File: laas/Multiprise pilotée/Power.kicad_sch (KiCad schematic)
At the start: 16 parts, among them J1 Conn_01x03, J2 Conn_01x02, J3 Conn_01x02, J4 Conn_01x02, J5 Conn_01x02, J6 Conn_01x03, K1 Omron Relay, K2 Omron Relay, K3 Omron Relay, K4 Omron Relay, U1 MAX4820xUP, U3 TPS75933KC

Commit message: Sauvegarde du travail en cours
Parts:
- J2: footprint Connector_Wago:Wago_734-132_1x02_P3.50mm_Vertical -> Connector_Wuerth:Wuerth_WR-WTB_64800211622_1x02_P1.50mm_Vertical
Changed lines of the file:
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@@
       (effects (font (size 1.27 1.27)) hide)
     )
-    (property "Footprint" "Connector_Wago:Wago_734-132_1x02_P3.50mm_Vertical" (at 170.18 139.7 0)
+    (property "Footprint" "Connector_Wuerth:Wuerth_WR-WTB_64800211622_1x02_P1.50mm_Vertical" (at 170.18 139.7 0)
       (effects (font (size 1.27 1.27)) hide)
     )

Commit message: Commit de propreté
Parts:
- C1: footprint Capacitor_THT:CP_Radial_D6.3mm_P2.50mm -> Capacitor_THT:CP_Radial_D5.0mm_P2.00mm
- J1, J6: footprint Connector_Wago:Wago_734-133_1x03_P3.50mm_Vertical -> Borniers:5442183
- J2: footprint Connector_Wuerth:Wuerth_WR-WTB_64800211622_1x02_P1.50mm_Vertical -> Borniers:5442170
- J3, J4, J5: footprint Connector_Wago:Wago_734-132_1x02_P3.50mm_Vertical -> Borniers:5442170
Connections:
- net Relay_1: now also U1.19 (OUT2); no longer U1.20 (OUT1)
- net Relay_2: now also U1.16 (OUT4); no longer U1.19 (OUT2)
- net Relay_4: now also U1.20 (OUT1); no longer U1.16 (OUT4)
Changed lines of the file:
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@@
     (stroke (width 0) (type default))
-  )
-  (label "Relay_1" (at 99.06 101.6 180) (fields_autoplaced)
-    (effects (font (size 1.27 1.27)) (justify right bottom))
-  )
-  (label "Relay_2" (at 99.06 104.14 180) (fields_autoplaced)
-    (effects (font (size 1.27 1.27)) (justify right bottom))
   )
   (label "Relay_4" (at 242.57 109.22 90) (fields_autoplaced)
@@
     (effects (font (size 1.27 1.27)) (justify left bottom))
   )
+  (label "Relay_1" (at 99.06 104.14 180) (fields_autoplaced)
+    (effects (font (size 1.27 1.27)) (justify right bottom))
+  )
+  (label "Relay_2" (at 99.06 109.22 180) (fields_autoplaced)
+    (effects (font (size 1.27 1.27)) (justify right bottom))
+  )
   (label "Relay_3" (at 213.36 109.22 90) (fields_autoplaced)
     (effects (font (size 1.27 1.27)) (justify left bottom))
   )
-  (label "Relay_4" (at 99.06 109.22 180) (fields_autoplaced)
+  (label "Relay_4" (at 99.06 101.6 180) (fields_autoplaced)
     (effects (font (size 1.27 1.27)) (justify right bottom))
   )
@@
       (effects (font (size 1.27 1.27)) hide)
     )
-    (property "Footprint" "Connector_Wago:Wago_734-132_1x02_P3.50mm_Vertical" (at 261.62 139.7 0)
+    (property "Footprint" "Borniers:5442170" (at 261.62 139.7 0)
       (effects (font (size 1.27 1.27)) hide)
     )
@@
       (effects (font (size 1.27 1.27)) (justify left))
     )
-    (property "Footprint" "Capacitor_THT:CP_Radial_D6.3mm_P2.50mm" (at 157.1752 45.72 0)
+    (property "Footprint" "Capacitor_THT:CP_Radial_D5.0mm_P2.00mm" (at 157.1752 45.72 0)
       (effects (font (size 1.27 1.27)) hide)
     )
@@
       (effects (font (size 1.27 1.27)) hide)
     )
-    (property "Footprint" "Connector_Wago:Wago_734-133_1x03_P3.50mm_Vertical" (at 30.48 40.64 0)
+    (property "Footprint" "Borniers:5442183" (at 30.48 40.64 0)
       (effects (font (size 1.27 1.27)) hide)
     )
@@
       (effects (font (size 1.27 1.27)) hide)
     )
-    (property "Footprint" "Connector_Wago:Wago_734-132_1x02_P3.50mm_Vertical" (at 231.14 139.7 0)
+    (property "Footprint" "Borniers:5442170" (at 231.14 139.7 0)
       (effects (font (size 1.27 1.27)) hide)
     )
@@
       (effects (font (size 1.27 1.27)) hide)
     )
-    (property "Footprint" "Connector_Wago:Wago_734-132_1x02_P3.50mm_Vertical" (at 201.93 139.7 0)
+    (property "Footprint" "Borniers:5442170" (at 201.93 139.7 0)
       (effects (font (size 1.27 1.27)) hide)
     )
@@
       (effects (font (size 1.27 1.27)) hide)
     )
-    (property "Footprint" "Connector_Wago:Wago_734-133_1x03_P3.50mm_Vertical" (at 30.48 54.61 0)
+    (property "Footprint" "Borniers:5442183" (at 30.48 54.61 0)
       (effects (font (size 1.27 1.27)) hide)
     )
@@
       (effects (font (size 1.27 1.27)) hide)
     )
-    (property "Footprint" "Connector_Wuerth:Wuerth_WR-WTB_64800211622_1x02_P1.50mm_Vertical" (at 170.18 139.7 0)
-      (effects (font (size 1.27 1.27)) hide)
-    )
+    (property "Footprint" "Borniers:5442170" (at 170.18 139.7 0)
+      (effects (font (size 1.27 1.27)) hide)
+    )

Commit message: Doc api
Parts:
- added H1, H2, H3, H4: MountingHole, MountingHole:MountingHole_4.3mm_M4, symbol Mechanical:MountingHole
- PS2: value MPM-45 -> MPM-30-5; footprint Multiprise pilotée:Converter_ACDC_MeanWell_MPM-45-xx_THT -> Multiprise pilotée:Converter_ACDC_MeanWell_MPM-30-xx_THT
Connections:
- net +5V: now also U1.2 (~{SET})
- net R3_L: now reaches J4.1 (Pin_1), K3.14
- net R3_N: now reaches J4.2 (Pin_2), K3.24
- net R1_L: now reaches J2.1 (Pin_1), K1.14
- net R1_N: now reaches J2.2 (Pin_2), K1.24
- net R4_L: now reaches J5.1 (Pin_1), K4.14
- net R4_N: now reaches J5.2 (Pin_2), K4.24
- net R2_L: now reaches J3.1 (Pin_1), K2.14
- net R2_N: now reaches J3.2 (Pin_2), K2.24
- no-connect marks 14 -> 13
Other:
- title: (none) -> AC & Relay
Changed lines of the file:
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@@
 (kicad_sch (version 20230121) (generator eeschema)
   (paper "A4")
+  (title_block
+    (title "AC & Relay")
+    (date "2024-04-26")
+    (rev "1.2")
+  )
   (junction (at 39.37 52.07) (diameter 0) (color 0 0 0 0)
   )
@@
   (no_connect (at 81.28 111.76))
   (no_connect (at 176.53 106.68))
-  (no_connect (at 55.88 104.14))
   (no_connect (at 266.7 116.84))
   (no_connect (at 207.01 116.84))
@@
     (stroke (width 0) (type default))
   )
+  (wire (pts (xy 49.53 104.14) (xy 49.53 87.63))
+    (stroke (width 0) (type default))
+  )
   (wire (pts (xy 81.28 109.22) (xy 99.06 109.22))
     (stroke (width 0) (type default))
@@
     (stroke (width 0) (type default))
   )
+  (wire (pts (xy 49.53 87.63) (xy 68.58 87.63))
+    (stroke (width 0) (type default))
+  )
   (wire (pts (xy 152.4 99.06) (xy 152.4 109.22))
     (stroke (width 0) (type default))
@@
     (stroke (width 0) (type default))
   )
+  (wire (pts (xy 55.88 104.14) (xy 49.53 104.14))
+    (stroke (width 0) (type default))
+  )
   (wire (pts (xy 245.11 91.44) (xy 245.11 119.38))
     (stroke (width 0) (type default))
@@
   (wire (pts (xy 161.29 99.06) (xy 152.4 99.06))
     (stroke (width 0) (type default))
+  )
+  (label "R3_N" (at 228.6 134.62 90) (fields_autoplaced)
+    (effects (font (size 1.27 1.27)) (justify left bottom))
   )
   (label "Relay_4" (at 242.57 109.22 90) (fields_autoplaced)
     (effects (font (size 1.27 1.27)) (justify left bottom))
   )
+  (label "R4_N" (at 259.08 134.62 90) (fields_autoplaced)
+    (effects (font (size 1.27 1.27)) (justify left bottom))
+  )
+  (label "R1_N" (at 167.64 134.62 90) (fields_autoplaced)
+    (effects (font (size 1.27 1.27)) (justify left bottom))
+  )
+  (label "R4_L" (at 269.24 132.08 0) (fields_autoplaced)
+    (effects (font (size 1.27 1.27)) (justify left bottom))
+  )
   (label "Relay_1" (at 152.4 109.22 90) (fields_autoplaced)
     (effects (font (size 1.27 1.27)) (justify left bottom))
   )
+  (label "R1_L" (at 179.07 132.08 0) (fields_autoplaced)
+    (effects (font (size 1.27 1.27)) (justify left bottom))
+  )
   (label "Relay_3" (at 99.06 106.68 180) (fields_autoplaced)
     (effects (font (size 1.27 1.27)) (justify right bottom))
@@
     (effects (font (size 1.27 1.27)) (justify left bottom))
   )
+  (label "R2_L" (at 210.82 132.08 0) (fields_autoplaced)
+    (effects (font (size 1.27 1.27)) (justify left bottom))
+  )
   (label "Relay_1" (at 99.06 104.14 180) (fields_autoplaced)
     (effects (font (size 1.27 1.27)) (justify right bottom))
@@
     (effects (font (size 1.27 1.27)) (justify right bottom))
   )
+  (label "R3_L" (at 238.76 132.08 0) (fields_autoplaced)
+    (effects (font (size 1.27 1.27)) (justify left bottom))
+  )
+  (label "R2_N" (at 199.39 134.62 90) (fields_autoplaced)
+    (effects (font (size 1.27 1.27)) (justify left bottom))
+  )
   (hierarchical_label "~{CS_Relay}" (shape input) (at 43.18 114.3 180) (fields_autoplaced)
     (effects (font (size 1.27 1.27)) (justify right))
@@
         (path "/ad17dd83-c10a-426e-803d-3b2dda0cc379/ff439e0e-b879-40be-a702-6e5da693c895"
           (reference "#PWR04") (unit 1)
+        )
+      )
+    )
+  )
+  (symbol (lib_id "Mechanical:MountingHole") (at 36.83 194.31 0) (unit 1)
+    (in_bom yes) (on_board yes) (dnp no) (fields_autoplaced)
+    (property "Reference" "H4" (at 39.37 193.04 0)
+      (effects (font (size 1.27 1.27)) (justify left))
+    )
+    (property "Value" "MountingHole" (at 39.37 195.58 0)
+      (effects (font (size 1.27 1.27)) (justify left) hide)
+    )
+    (property "Footprint" "MountingHole:MountingHole_4.3mm_M4" (at 36.83 194.31 0)
+      (effects (font (size 1.27 1.27)) hide)
+    )
+    (property "Datasheet" "~" (at 36.83 194.31 0)
+      (effects (font (size 1.27 1.27)) hide)
+    )
+    (instances
+      (project "Multiprise pilotée"
+        (path "/ad17dd83-c10a-426e-803d-3b2dda0cc379/ff439e0e-b879-40be-a702-6e5da693c895"
+          (reference "H4") (unit 1)
         )
       )
@@
     )
   )
+  (symbol (lib_id "Mechanical:MountingHole") (at 36.83 184.15 0) (unit 1)
+    (in_bom yes) (on_board yes) (dnp no) (fields_autoplaced)
+    (property "Reference" "H2" (at 39.37 182.88 0)
+      (effects (font (size 1.27 1.27)) (justify left))
+    )
+    (property "Value" "MountingHole" (at 39.37 185.42 0)
+      (effects (font (size 1.27 1.27)) (justify left) hide)
+    )
+    (property "Footprint" "MountingHole:MountingHole_4.3mm_M4" (at 36.83 184.15 0)
+      (effects (font (size 1.27 1.27)) hide)
+    )
+    (property "Datasheet" "~" (at 36.83 184.15 0)
+      (effects (font (size 1.27 1.27)) hide)
+    )
+    (instances
+      (project "Multiprise pilotée"
+        (path "/ad17dd83-c10a-426e-803d-3b2dda0cc379/ff439e0e-b879-40be-a702-6e5da693c895"
+          (reference "H2") (unit 1)
+        )
+      )
+    )
+  )
   (symbol (lib_id "Connector_Generic:Conn_01x02") (at 261.62 139.7 270) (unit 1)
     (in_bom yes) (on_board yes) (dnp no) (fields_autoplaced)
@@
       (effects (font (size 1.27 1.27)))
     )
-    (property "Value" "MPM-45" (at 58.42 34.29 0)
-      (effects (font (size 1.27 1.27)))
-    )
-    (property "Footprint" "Multiprise pilotée:Converter_ACDC_MeanWell_MPM-45-xx_THT" (at 58.42 48.26 0)
+    (property "Value" "MPM-30-5" (at 58.42 34.29 0)
+      (effects (font (size 1.27 1.27)))
+    )
+    (property "Footprint" "Multiprise pilotée:Converter_ACDC_MeanWell_MPM-30-xx_THT" (at 58.42 48.26 0)
       (effects (font (size 1.27 1.27)) hide)
     )
@@
     )
   )
+  (symbol (lib_id "Mechanical:MountingHole") (at 36.83 189.23 0) (unit 1)
+    (in_bom yes) (on_board yes) (dnp no) (fields_autoplaced)
+    (property "Reference" "H3" (at 39.37 187.96 0)
+      (effects (font (size 1.27 1.27)) (justify left))
+    )
+    (property "Value" "MountingHole" (at 39.37 190.5 0)
+      (effects (font (size 1.27 1.27)) (justify left) hide)
+    )
+    (property "Footprint" "MountingHole:MountingHole_4.3mm_M4" (at 36.83 189.23 0)
+      (effects (font (size 1.27 1.27)) hide)
+    )
+    (property "Datasheet" "~" (at 36.83 189.23 0)
+      (effects (font (size 1.27 1.27)) hide)
+    )
+    (instances
+      (project "Multiprise pilotée"
+        (path "/ad17dd83-c10a-426e-803d-3b2dda0cc379/ff439e0e-b879-40be-a702-6e5da693c895"
+          (reference "H3") (unit 1)
+        )
+      )
+    )
+  )
   (symbol (lib_id "Multiprise pilotée:TPS75933KC") (at 124.46 40.64 0) (unit 1)
     (in_bom yes) (on_board yes) (dnp no) (fields_autoplaced)
@@
         )
       )
+    )
+  )
+  (symbol (lib_id "Mechanical:MountingHole") (at 36.83 179.07 0) (unit 1)
+    (in_bom yes) (on_board yes) (dnp no) (fields_autoplaced)
+    (property "Reference" "H1" (at 39.37 177.8 0)
+      (effects (font (size 1.27 1.27)) (justify left))
+    )
+    (property "Value" "MountingHole" (at 39.37 180.34 0)
+      (effects (font (size 1.27 1.27)) (justify left) hide)
+    )
+    (property "Footprint" "MountingHole:MountingHole_4.3mm_M4" (at 36.83 179.07 0)
+      (effects (font (size 1.27 1.27)) hide)
+    )
+    (property "Datasheet" "~" (at 36.83 179.07 0)
+      (effects (font (size 1.27 1.27)) hide)
+    )
+    (instances
+      (project "Multiprise pilotée"
+        (path "/ad17dd83-c10a-426e-803d-3b2dda0cc379/ff439e0e-b879-40be-a702-6e5da693c895"
+          (reference "H1") (unit 1)
+        )
+      )

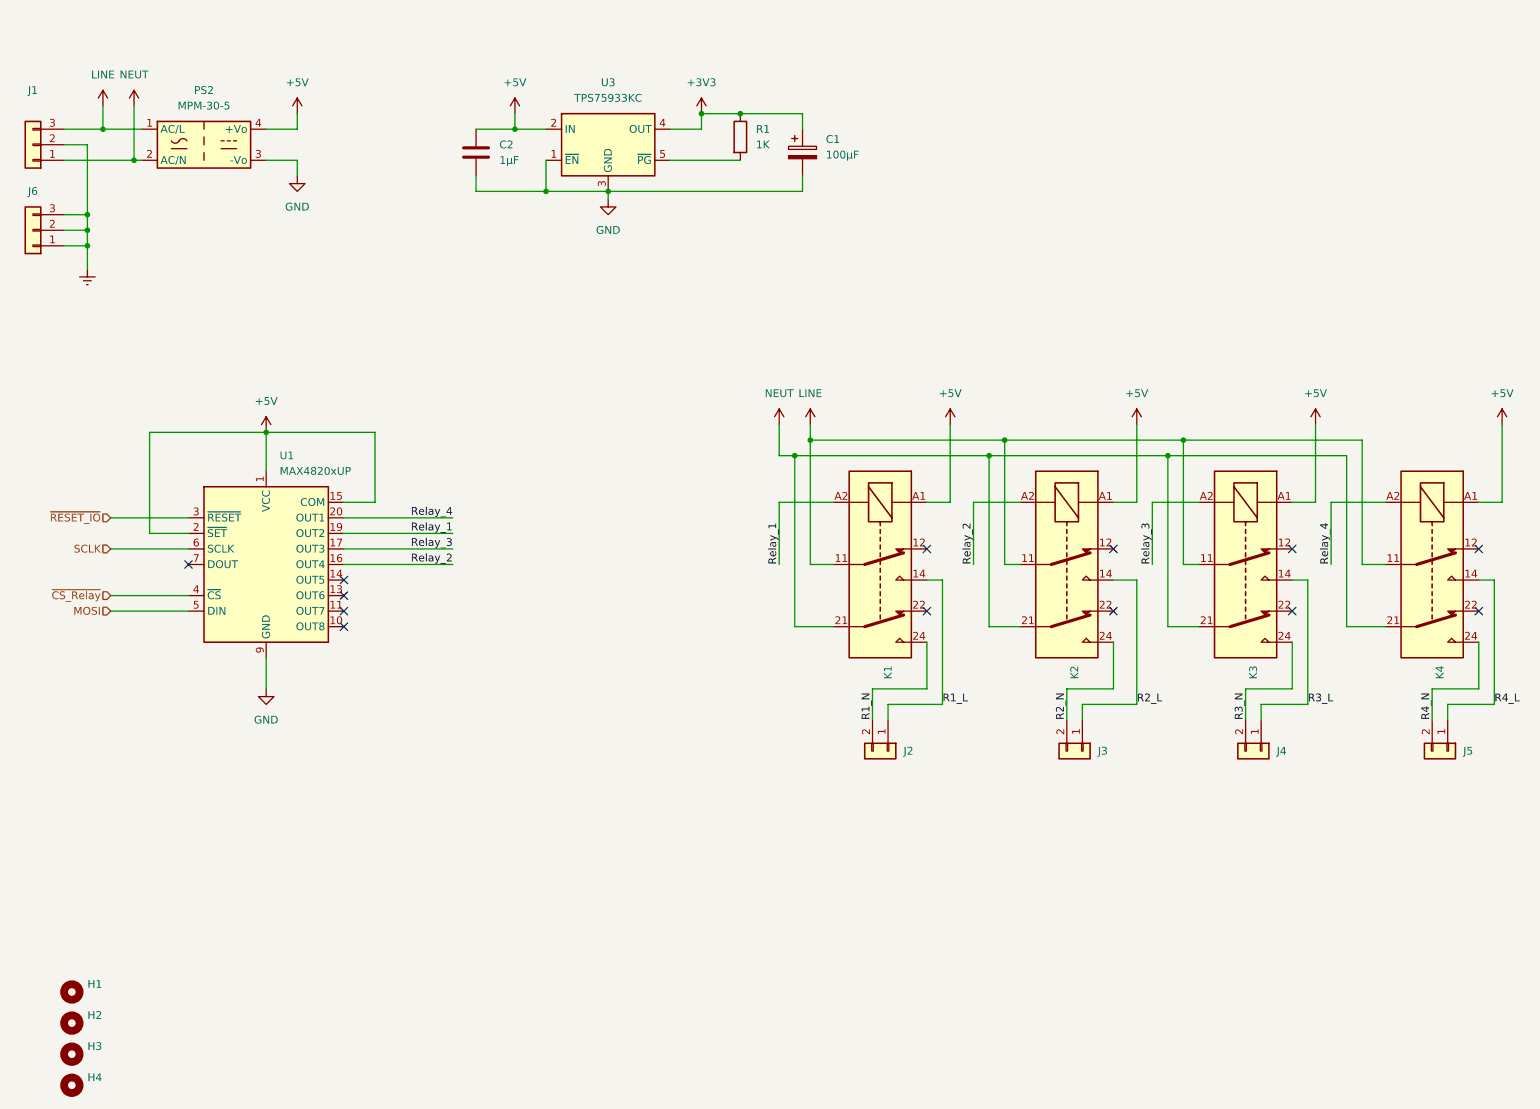
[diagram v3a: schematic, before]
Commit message: Nouvelle version PCB multiprise 1.3 avec suppresion des alim vpol et var
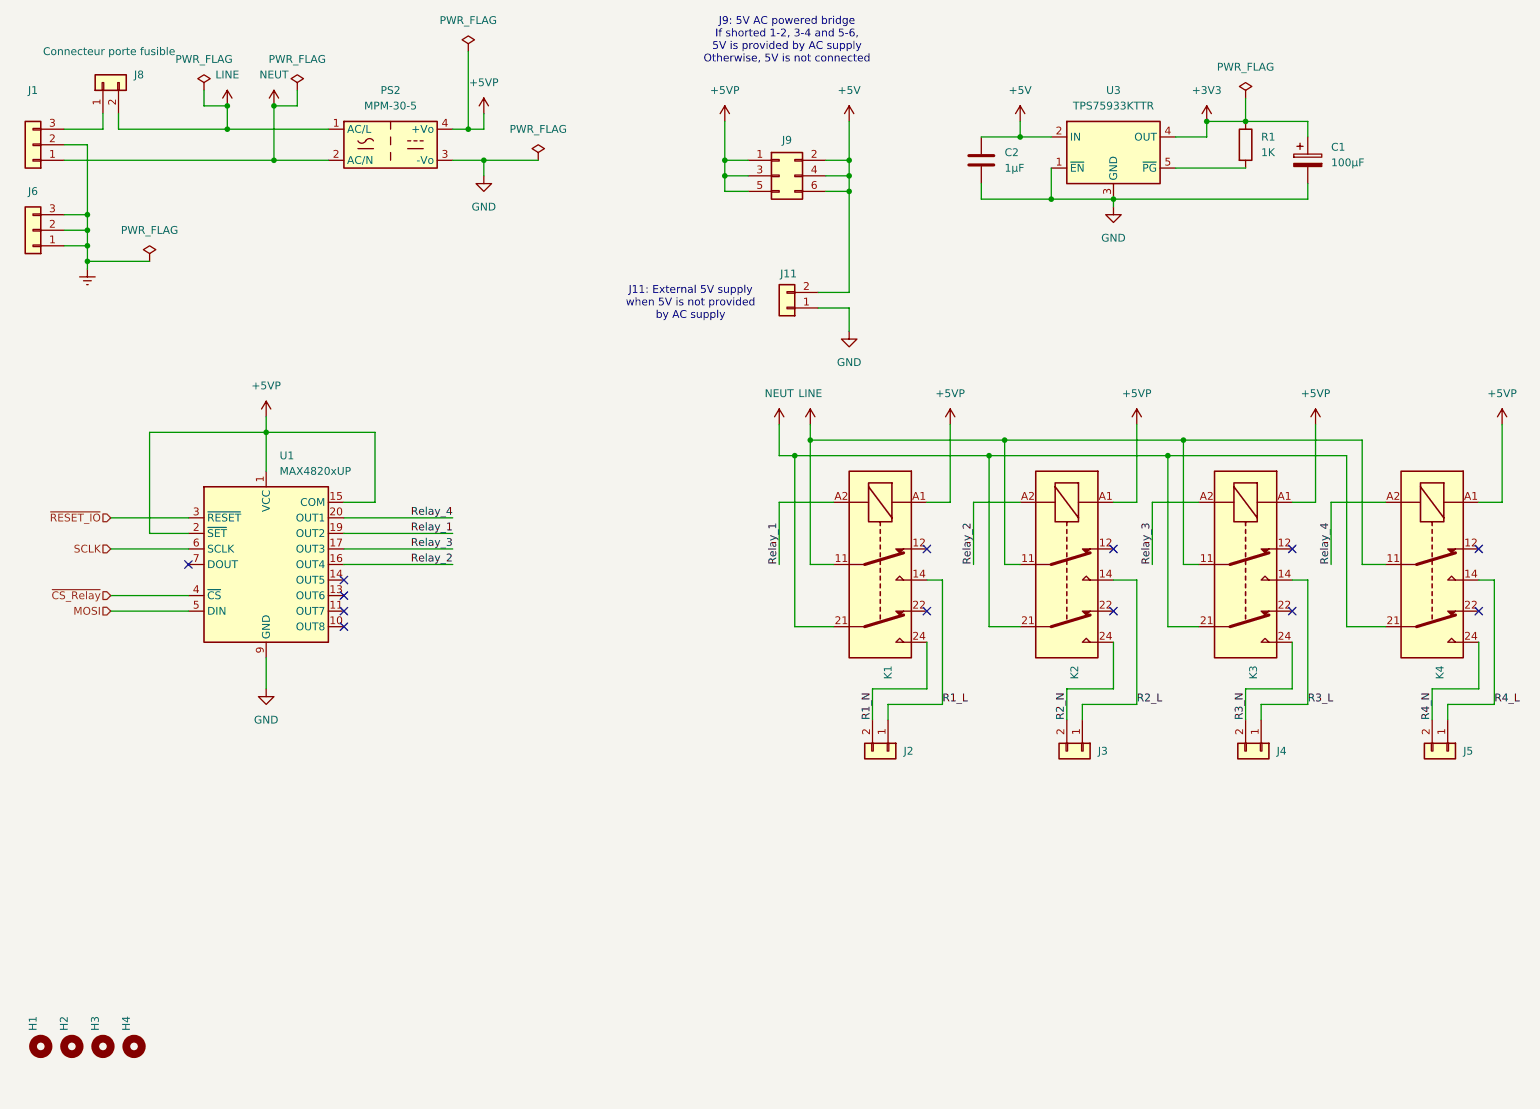
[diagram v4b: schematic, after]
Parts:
- added J11: Conn_01x02, Connector_PinHeader_2.54mm:PinHeader_1x02_P2.54mm_Vertical, symbol Connector_Generic:Conn_01x02
- added J8: Conn_01x02, Connector_Phoenix_MSTB:PhoenixContact_MSTBVA_2,5_2-G-5,08_1x02_P5.08mm_Vertical, symbol Connector_Generic:Conn_01x02
- added J9: Conn_02x03_Odd_Even, Connector_PinHeader_2.54mm:PinHeader_2x03_P2.54mm_Vertical, symbol Connector_Generic:Conn_02x03_Odd_Even
- J1, J6: footprint Borniers:5442183 -> Connector_Phoenix_MSTB:PhoenixContact_MSTBVA_2,5_3-G-5,08_1x03_P5.08mm_Vertical
- J2, J3, J4, J5: footprint Borniers:5442170 -> Connector_Phoenix_MSTB:PhoenixContact_MSTBVA_2,5_2-G-5,08_1x02_P5.08mm_Vertical
- U3: value TPS75933KC -> TPS75933KTTR
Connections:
- net +5V: now also J11.2 (Pin_2), J9.2 (Pin_2), J9.4 (Pin_4), J9.6 (Pin_6); no longer K1.A1, K2.A1, K3.A1, K4.A1, PS2.4 (+Vo), U1.1 (VCC), U1.15 (COM), U1.2 (~{SET})
- net GND: now also J11.1 (Pin_1)
- net LINE: now also J8.2 (Pin_2); no longer J1.3 (Pin_3)
- new net: J1.3 (Pin_3), J8.1 (Pin_1)
- new net +5VP: J9.1 (Pin_1), J9.3 (Pin_3), J9.5 (Pin_5), K1.A1, K2.A1, K3.A1, K4.A1, PS2.4 (+Vo), U1.1 (VCC), U1.15 (COM), U1.2 (~{SET})
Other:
- note added: "J11: External 5V supply when 5V is not provided by AC supply"
- note added: "J9: 5V AC powered bridge If shorted 1-2, 3-4 and 5-6, 5V is provided by AC supply Otherwise, 5V is not connected"
- company: (none) -> INSA -GEI
- title: AC & Relay -> Multiprise - AC & Relay
- moved on the sheet: C1, C2, H1, H2, H3, H4, PS2, R1, U3
